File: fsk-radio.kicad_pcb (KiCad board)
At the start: 4 copper layers, 62.5 x 25 mm, 86 parts, among them IC1 STM32F4xx-QFN48, IC2 AT86RF215, IC3 LM3671, IC4 LSM6DS3, IC5 CAT24-SOT23, IC7 DPX202700DT, IC8 74AHC2G04, J1 USB_A, J2 CONN_01X14, J3 CONN_02X05, J4 RF_Shield_One_Piece, J7 SMA, X1 TXETBLSANF-26, X2 32.768kHz

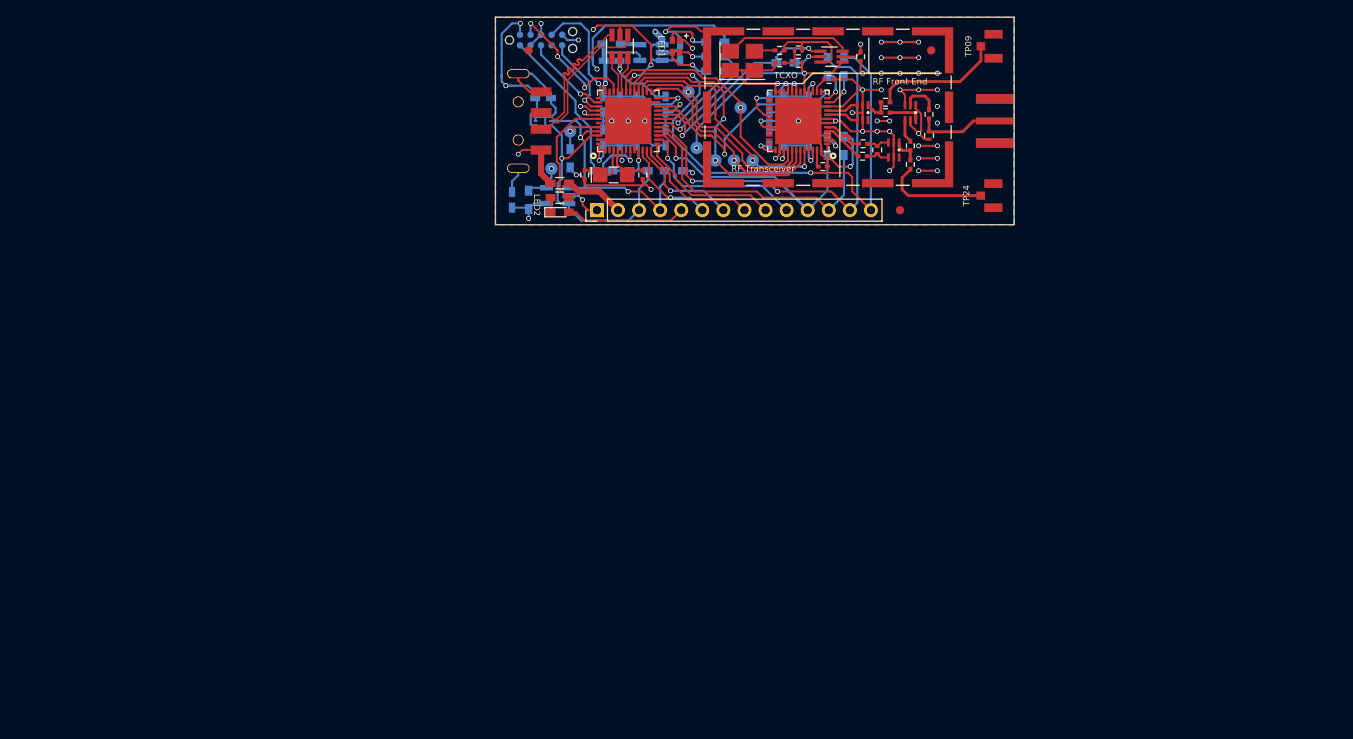
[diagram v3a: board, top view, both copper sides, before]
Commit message: Rework and revise for revision 2.
Major changes include:
  - Refactor clock heirarchy to improve RF performance.
  - Add pushbutton switch and SPI flash.
  - Shrink board dimensions down to make it more of a usable dongle.
  - Eliminate u.FL test points and SPI test pads.
  - Convert pin headers to castellated edges.
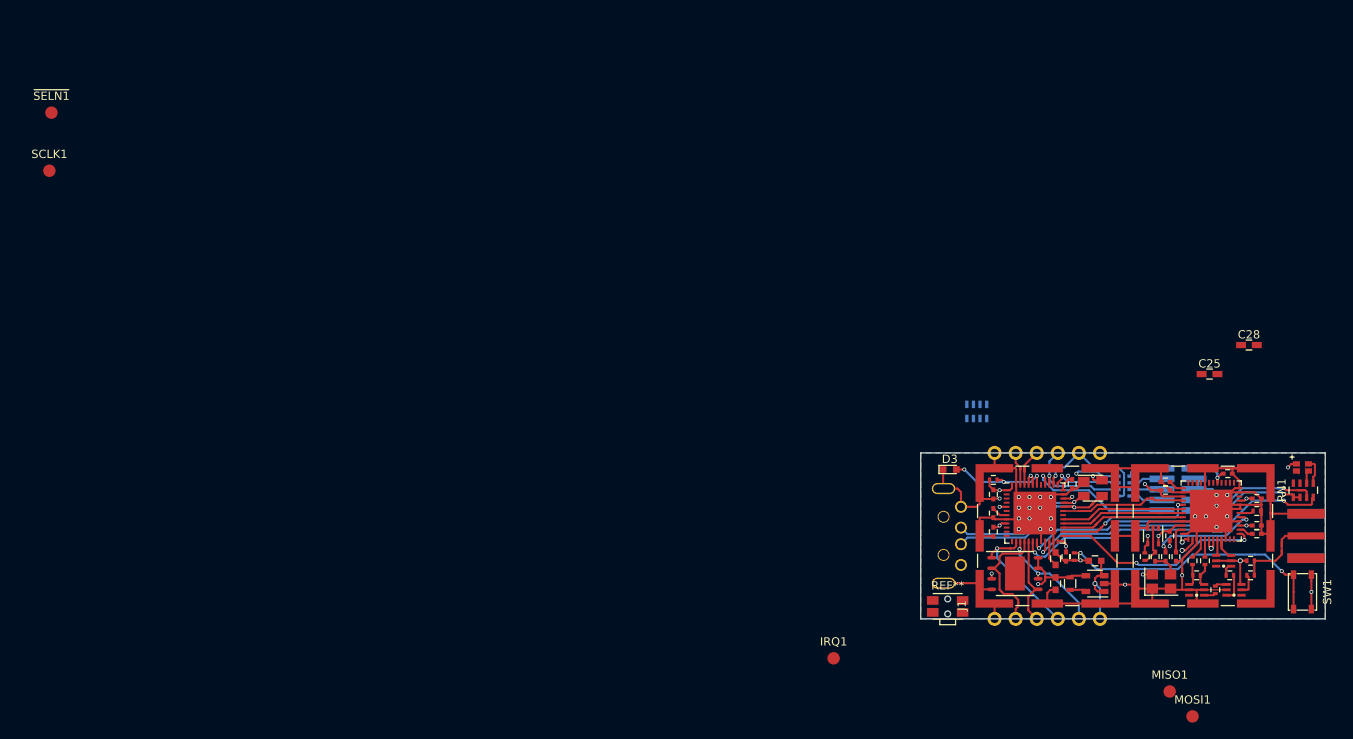
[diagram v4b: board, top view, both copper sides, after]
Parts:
- removed BOOT: BOOT, Measurement_Points:Measurement_Point_Round-SMD-Pad_Small
- removed C1, C2: 1u, Capacitors_SMD:C_0603_HandSoldering
- removed C12, C13, C14, C30: C, Capacitors_SMD:C_0402
- removed C16: C, Capacitors_SMD:C_0603_HandSoldering
- removed IC5: CAT24-SOT23, TO_SOT_Packages_SMD:SOT-23-5_HandSoldering
- removed IC8: 74AHC2G04, TO_SOT_Packages_SMD:SOT-363_SC-70-6_Handsoldering
- removed IRQ, MISO, MOSI, SCLK, TCXO, ~CSEL: TEST, Measurement_Points:Measurement_Point_Round-SMD-Pad_Small
- removed R10, R11: 4.7k, Resistors_SMD:R_0603_HandSoldering
- removed R12, R13: 470k, Resistors_SMD:R_0402
- removed R14, R9: 100k, Resistors_SMD:R_0603_HandSoldering
- removed R15, R16, R18, R19: 0, Resistors_SMD:R_0603_HandSoldering
- removed R6, R7: 270, Resistors_SMD:R_0603_HandSoldering
- removed R8: 100, Resistors_SMD:R_0603_HandSoldering
- removed the REF** at (101.2, 41.5)
- removed the REF** at (146.0, 60.8)
- removed the REF** at (149.8, 41.5)
- removed TP09, TP24: u.FL, FSK Parts:u.FL
- removed WP: WP, Measurement_Points:Measurement_Point_Round-SMD-Pad_Small
- removed X2: 32.768kHz, Crystals:Crystal_SMD_G8-2pin_3.2x1.5mm_HandSoldering
- added IC6: W25Q32BVZPIP, Housings_DFN_QFN:DFN-S-8-1EP_6x5mm_Pitch1.27mm, F.Cu at (159.8, 104.5)
- added IRQ1: TEST, Measurement_Points:Measurement_Point_Round-SMD-Pad_Small, F.Cu at (138.0, 114.8)
- added J5: RF_Shield_One_Piece, Shielding_Cabinets:Laird_Technologies_BMI-S-102_16.50x16.50mm, F.Cu at (163.8, 100.0)
- added J6: Conn_01x06, FSK Parts:Castellated_Edge_6pin_2.54mm, F.Cu at (163.8, 110.0)
- added MISO1: TEST, Measurement_Points:Measurement_Point_Round-SMD-Pad_Small, F.Cu at (178.5, 118.8)
- added MOSI1: TEST, Measurement_Points:Measurement_Point_Round-SMD-Pad_Small, F.Cu at (181.2, 121.8)
- added REF**: SW_SPST_EVQP7C, Buttons_Switches_SMD:SW_SPST_EVQP7C, F.Cu at (151.8, 108.5)
- added RN1: 330, Resistors_SMD:R_Array_Concave_4x0603, F.Cu at (194.6, 94.5)
- added RN2: 4.7k, Resistors_SMD:R_Array_Concave_4x0603, B.Cu at (155.2, 85.0)
- added RN3: 22, Resistors_SMD:R_Array_Concave_4x0603, B.Cu at (173.0, 94.0)
- added SCLK1: TEST, Measurement_Points:Measurement_Point_Round-SMD-Pad_Small, F.Cu at (43.5, 56.0)
- added SW1: SW_Push, Buttons_Switches_SMD:SW_SPST_PTS810, F.Cu at (194.5, 106.8)
- added ~SELN1: TEST, Measurement_Points:Measurement_Point_Round-SMD-Pad_Small, F.Cu at (43.8, 49.0)
- C10, C18, C21, C22, C23, C24, C5, C6, C8: footprint Capacitors_SMD:C_0603_HandSoldering -> Capacitors_SMD:C_0402; moved to F.Cu
- C11: value 2.2u -> 4.7u; footprint Capacitors_SMD:C_0603_HandSoldering -> Capacitors_SMD:C_0603; moved to F.Cu
- C25, C28: moved to F.Cu
- C26, C27, C29, C31, C32: footprint Capacitors_SMD:C_0402 -> Inductors_SMD:L_0402
- C3, C7: footprint Capacitors_SMD:C_0603_HandSoldering -> Capacitors_SMD:C_0603; moved to F.Cu
- C9: value 2.2u -> 1n; footprint Capacitors_SMD:C_0603_HandSoldering -> Capacitors_SMD:C_0402; moved to F.Cu
- D2: value ESDALCL6 -> PRTR5V0U2X; footprint TO_SOT_Packages_SMD:SOT-23-6_Handsoldering -> TO_SOT_Packages_SMD:SOT-143
- D3: footprint LEDs:LED_0603_HandSoldering -> LEDs:LED_0603
- IC1, IC2: footprint FSK Parts:QFN48 -> Housings_DFN_QFN:QFN-48-1EP_7x7mm_Pitch0.5mm
- IC3: footprint TO_SOT_Packages_SMD:SOT-23-5_HandSoldering -> TO_SOT_Packages_SMD:SOT-23-5; moved to F.Cu
- IC4: value LSM6DS3 -> NC7SZ04; footprint FSK Parts:LGA-14 -> TO_SOT_Packages_SMD:SOT-353_SC-70-5; moved to F.Cu
- J1: footprint FSK Parts:USB-A-Plug -> FSK Parts:CUI-UP2-AH-TH
- J2: value CONN_01X14 -> Conn_01x06; footprint Pin_Headers:Pin_Header_Straight_1x14_Pitch2.54mm -> FSK Parts:Castellated_Edge_6pin_2.54mm; moved to B.Cu
- J3: footprint Connectors:Tag-Connect_TC2050-IDC-NL -> FSK Parts:ftsh-105-01-dv
- J4: footprint Shielding_Cabinets:Laird_Technologies_BMI-S-209-F_29.36x18.50mm -> Shielding_Cabinets:Laird_Technologies_BMI-S-102_16.50x16.50mm
- L1: footprint Inductors_SMD:L_0603_HandSoldering -> Inductors_SMD:L_0603; moved to F.Cu
- R1: value 0 -> 10k; footprint Resistors_SMD:R_0603_HandSoldering -> Resistors_SMD:R_0402
- R2: footprint Resistors_SMD:R_0603_HandSoldering -> Resistors_SMD:R_0402
- R3, R4: value 100k -> R; footprint Resistors_SMD:R_0603_HandSoldering -> Resistors_SMD:R_0402; moved to F.Cu
- X1: footprint Crystals:Crystal_SMD_TXC_7M-4pin_3.2x2.5mm_HandSoldering -> Crystals:Crystal_SMD_3225-4pin_3.2x2.5mm
- moved J3 93.9 mm to (179.5, 94.4), turned to 180 degrees
- moved D1 91.0 mm to (194.5, 91.8), turned to 270 degrees
- moved C18 89.0 mm to (178.5, 100.0), turned to 270 degrees
- moved IC4 88.9 mm to (176.5, 100.0), turned to 270 degrees
- moved R4 88.8 mm to (189.0, 97.0), turned to 0 degrees
- moved C10 88.2 mm to (189.0, 98.8), turned to 0 degrees
- moved L1 85.3 mm to (166.5, 105.8), turned to 90 degrees
- moved IC3 83.4 mm to (169.5, 105.8)
- moved C3 82.7 mm to (164.8, 105.8), turned to 270 degrees
- moved X1 80.5 mm to (177.5, 105.5)
- moved C7 79.1 mm to (169.5, 103.0), turned to 180 degrees
- moved D2 78.0 mm to (169.2, 94.2), turned to 0 degrees
- moved C9 77.7 mm to (176.8, 102.5)
- moved C15 76.7 mm to (178.0, 102.5), turned to 270 degrees
- moved R1 76.6 mm to (167.0, 102.5), turned to 270 degrees
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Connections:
- C15 pad 1: Net-(C15-Pad1) -> /CPU/RF_CLK
- C4 pad 1: Net-(B24-Pad1) -> GND
- C9 pad 1: Net-(C11-Pad1) -> Net-(C9-Pad1)
- C9 pad 2: GND -> Net-(C15-Pad2)
- D2 pad 1: /CPU/USB+ -> GND
- D2 pad 2: GND -> /CPU/USB+
- D2 pad 4: /CPU/USBA- -> +5V
- D3 pad 1: Net-(D3-Pad1) -> GND
- D3 pad 2: VCC -> /CPU/STATUS
- IC1 pad 12: /CPU/PA2 -> Net-(IC1-Pad12)
- IC1 pad 13: /CPU/PA3 -> Net-(IC1-Pad13)
- IC1 pad 14: /CPU/PA4 -> /CPU/~FL_CSEL
- IC1 pad 15: /CPU/PA5 -> /CPU/FL_SCLK
- IC1 pad 16: /CPU/PA6 -> /CPU/FL_MISO
- IC1 pad 17: /CPU/PA7 -> /CPU/FL_MOSI
- IC1 pad 18: Net-(IC1-Pad18) -> /CPU/RED
- IC1 pad 19: Net-(IC1-Pad19) -> /CPU/GREEN
- IC1 pad 20: /CPU/~CLKEN -> GND
- IC1 pad 21: /CPU/~RF_NRST -> /CPU/BLUE
- IC1 pad 25: /CPU/~SPI_CS -> /CPU/~RF_NRST
- IC1 pad 29: /CPU/PA8 -> /CPU/~SPI_CS
- IC1 pad 30: Net-(D2-Pad5) -> +5V
- IC1 pad 38: Net-(IC1-Pad38) -> /CPU/TXD_OUT
- IC1 pad 39: Net-(IC1-Pad39) -> /CPU/RXD_IN
- IC1 pad 42: Net-(IC1-Pad42) -> /CPU/STATUS
- IC1 pad 43: Net-(IC1-Pad43) -> /CPU/SWITCH
- IC1 pad 44: Net-(BOOT1-Pad1) -> /CPU/SWITCH
- IC1 pad 5: TCXO -> Net-(IC1-Pad5)
- IC1 pad 7: ~NRST -> Net-(C4-Pad2)
- IC2 pad 17: TCXO -> /CPU/RF_CLK
- IC4 pad 1: GND -> (no net)
- IC4 pad 2: GND -> Net-(C9-Pad1)
- IC4 pad 4: Net-(IC4-Pad4) -> Net-(IC1-Pad5)
- J1 pad 1: Net-(D2-Pad5) -> +5V
- J1 pad 2: /CPU/USBA- -> /CPU/USB-
- J1 pad 3: /CPU/USBA+ -> /CPU/USB+
- J2 pad 2: +5V -> /CPU/SDA
- J2 pad 3: /CPU/SDA -> /CPU/SCL
- J2 pad 4: /CPU/SCL -> /CPU/RXD_IN
- J2 pad 5: VCC -> /CPU/TXD_OUT
- J2 pad 6: /CPU/PA0 -> VCC
- J3 pad 10: ~NRST -> Net-(IC1-Pad40)
- J3 pad 2: Net-(IC1-Pad34) -> Net-(J3-Pad2)
- J3 pad 4: Net-(IC1-Pad37) -> Net-(J3-Pad4)
- J3 pad 6: Net-(IC1-Pad39) -> Net-(J3-Pad6)
- J3 pad 8: Net-(IC1-Pad38) -> Net-(J3-Pad8)
- R1 pad 1: +5V -> /CPU/SWITCH
- R1 pad 2: Net-(D2-Pad5) -> GND
- R2 pad 1: Net-(D3-Pad1) -> VCC
- R2 pad 2: Net-(IC1-Pad42) -> /CPU/STATUS
- R3 pad 1: GND -> Net-(IC1-Pad5)
- R3 pad 2: /CPU/~CLKEN -> Net-(C9-Pad1)
- R4 pad 1: VCC -> Net-(IC2-Pad18)
- R4 pad 2: ~NRST -> GND
- X1 pad 3: Net-(C15-Pad1) -> Net-(C15-Pad2)
- X1 pad 4: Net-(IC8-Pad6) -> VCC
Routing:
- net /CPU/PA8: track 70.2 -> 0.00 mm, vias 2 -> 0
- net /CPU/PA7: track 51.5 -> 0.00 mm, vias 2 -> 0
- net /CPU/SWITCH: track 0.00 -> 49.4 mm, vias 0 -> 3
- net Net-(D2-Pad5): track 42.8 -> 0.00 mm, vias 4 -> 0
- net /CPU/RED: track 0.00 -> 39.0 mm, vias 0 -> 2
- net TCXO: track 38.9 -> 0.00 mm, vias 3 -> 0
- net /CPU/GREEN: track 0.00 -> 38.3 mm, vias 0 -> 2
- net /CPU/BLUE: track 0.00 -> 35.8 mm, vias 0 -> 2
- net /CPU/PA6: track 35.0 -> 0.00 mm
- net /CPU/PA5: track 34.6 -> 0.00 mm, vias 1 -> 0
- net GND: track 330.0 -> 296.2 mm, vias 49 -> 27
- net Net-(IC1-Pad41): track 30.7 -> 0.00 mm, vias 2 -> 0
- net /CPU/SDA: track 32.4 -> 4.33 mm, vias 1 -> 0
- net /CPU/~CLKEN: track 27.5 -> 0.00 mm, vias 2 -> 0
- net /CPU/SCL: track 31.2 -> 5.05 mm, vias 2 -> 0
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- removed copper zone on F.Cu, net GND
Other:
- board size 62.5 x 25 mm -> 48.8 x 20 mm
- net class Default: clearance 0.18 -> 0.175; via_dia 0.6 -> 0.475; via_drill 0.4 -> 0.3
- net class RF-50ohm removed
- net class RF-Diff removed
- net class USB: clearance 0.15 -> 0.16; trace_width 0.2 -> 0.25; via_dia 0.6 -> 0.475; via_drill 0.4 -> 0.3
- rule pad_to_mask_clearance: 0.05 -> 0
- rule trace_clearance: 0.18 -> 0.175
- rule trace_min: 0.15 -> 0.2
- board text added: "CSEL"
- board text added: "MISO"
- board text added: "MOSI"
- board text added: "RXD_IN"
- board text added: "SCLK"
- board text added: "TXD_OUT"
- board text added: "VUSB"
- board text removed: "+5V"
- board text removed: "A"
- board text removed: "B"
- board text removed: "Blue"
- board text removed: "C"
- board text removed: "CPU Bypass"
- board text removed: "Core Bypass"
- board text removed: "DC-DC Regulator"
- board text removed: "EEPROM"
- board text removed: "FEx09"
- board text removed: "FEx24"
- board text removed: "Green"
- board text removed: "IMU"
- board text removed: "JTAG"
- board text removed: "L"
- board text removed: "LED1"
- board text removed: "LED2"
- board text removed: "PA0"
- board text removed: "PA1"
- board text removed: "PA2"
- board text removed: "PA3"
- board text removed: "PA4"
- board text removed: "PA5"
- board text removed: "PA6"
- board text removed: "PA7"
- board text removed: "PA8"
- board text removed: "RF Bypass"
- board text removed: "RF Front End"
- board text removed: "RF Transceiver"
- board text removed: "Red"
- board text removed: "TCXO"
- board text removed: "https://github.com/oskirby/fsk-radio"

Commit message: Add more test features to the RF section.
Split the RF and CPU power nets and connect them via a zero-ohm jumper
to allow current sense, and add test pads for the RF SPI bus.
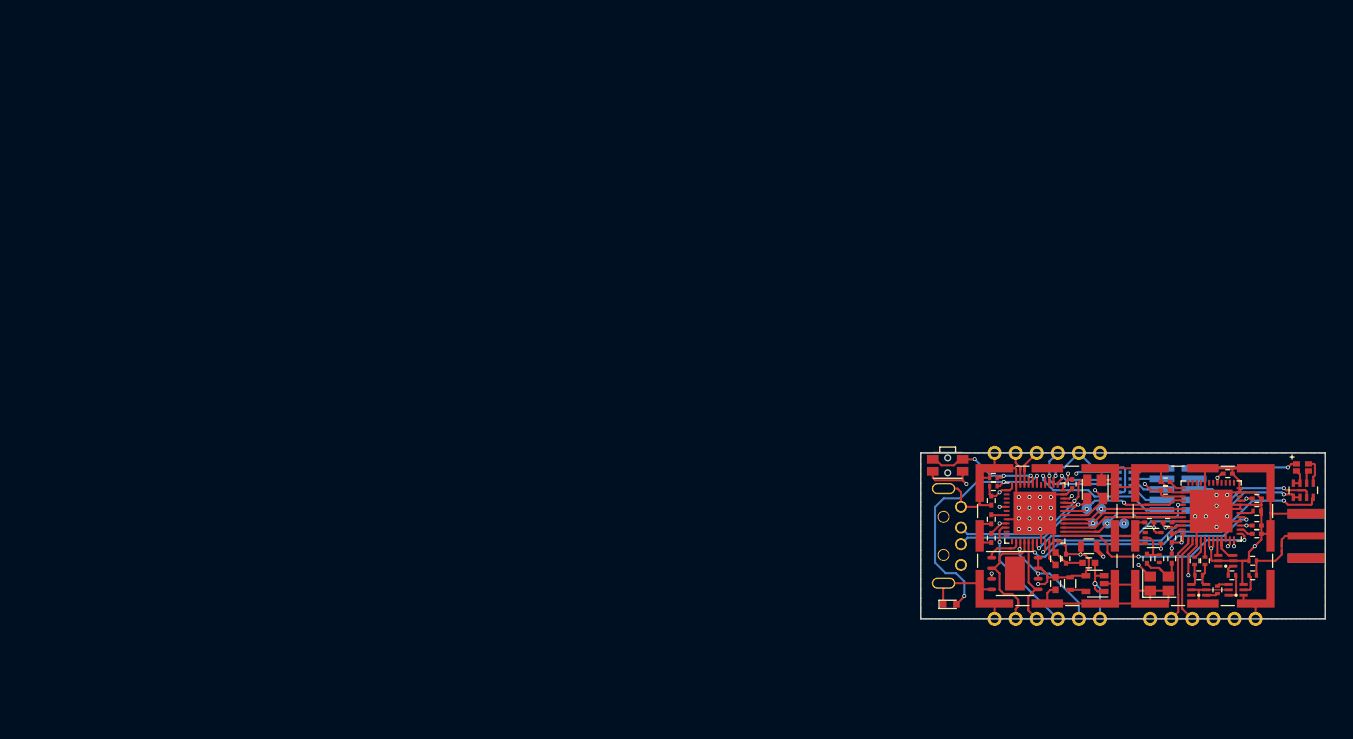
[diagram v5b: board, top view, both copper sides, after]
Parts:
- removed C18: C, Capacitors_SMD:C_0402
- removed REF**: SW_SPST_EVQP7C, Buttons_Switches_SMD:SW_SPST_EVQP7C
- removed RN2: 4.7k, Resistors_SMD:R_Array_Concave_4x0603
- added J8: Conn_01x06, FSK Parts:Castellated_Edge_6pin_2.54mm, F.Cu at (182.5, 110.0)
- added R5: 0, Resistors_SMD:R_0805, F.Cu at (168.8, 101.2)
- added exegin-logo: exegin-logo, FSK Parts:exegin-logo-mask, B.Cu at (193.2, 106.8)
- C25, C28: footprint Capacitors_SMD:C_0603_HandSoldering -> Capacitors_SMD:C_0402
- IRQ1, MISO1, MOSI1, SCLK1, ~SELN1: footprint Measurement_Points:Measurement_Point_Round-SMD-Pad_Small -> FSK Parts:Measurement_Point_Round-SMD-Pad_XSmall; moved to B.Cu
- SW1: footprint Buttons_Switches_SMD:SW_SPST_PTS810 -> Buttons_Switches_SMD:SW_SPST_EVQP7C
- moved ~SELN1 135.2 mm to (170.2, 96.8)
- moved SCLK1 134.4 mm to (171.0, 98.5)
- moved SW1 45.4 mm to (151.8, 91.5), turned to 180 degrees
- moved IRQ1 35.4 mm to (168.5, 96.8)
- moved MOSI1 26.2 mm to (169.2, 98.5)
- moved C10 23.3 mm to (166.0, 102.8), turned to 270 degrees
- moved MISO1 21.0 mm to (173.0, 98.5)
- moved C25 19.1 mm to (189.0, 98.8)
- moved C28 18.5 mm to (189.0, 95.5)
- moved D3 16.2 mm to (152.0, 108.2)
- moved R1 13.6 mm to (157.2, 93.0), turned to 180 degrees
- moved C17 13.3 mm to (176.1, 98.4), turned to 0 degrees
- moved C24 12.9 mm to (178.2, 98.4), turned to 0 degrees
- moved oshw-text 4.12 mm to (177.2, 106.5)
- moved oshw-silks 3.40 mm to (185.5, 105.5)
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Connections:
- net /CPU/PA1 renamed Net-(IC1-Pad11)
- C22 pad 1: VCC -> VDD
- C23 pad 1: VCC -> VDD
- C24 pad 1: VCC -> VDD
- C25 pad 1: VCC -> VDD
- C28 pad 1: VCC -> VDD
- IC1 pad 10: /CPU/PA0 -> /CPU/~EXT_CSEL
- IC2 pad 15: VCC -> VDD
- IC2 pad 21: VCC -> VDD
- IC2 pad 29: VCC -> VDD
- IC2 pad 39: VCC -> VDD
- IC2 pad 46: VCC -> VDD
- J6 pad 4: /CPU/~FL_CSEL -> /CPU/~EXT_CSEL
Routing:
- net VDD: track 0.00 -> 50.1 mm, vias 0 -> 6
- net /CPU/SWITCH: track 49.4 -> 16.9 mm
- net /CPU/STATUS: track 12.7 -> 30.3 mm
- net /CPU/~EXT_CSEL: track 0.00 -> 14.6 mm, vias 0 -> 1
- net /CPU/~FL_CSEL: track 16.8 -> 4.57 mm, vias 1 -> 0
- net VCC: track 149.8 -> 138.2 mm, vias 14 -> 10
- net /RF/FEA09: track 0.00 -> 10.4 mm, vias 0 -> 1
- net /RF/FEB09: track 0.00 -> 9.62 mm, vias 0 -> 1
- net /RF/FEA24: track 0.89 -> 10.5 mm, vias 1 -> 0
- net /RF/FEB24: track 2.10 -> 10.6 mm, vias 1 -> 0
- net GND: track 296.2 -> 289.5 mm, vias 27 -> 26
- net +5V: track 41.1 -> 46.4 mm
- net /CPU/USB+: track 18.1 -> 20.9 mm
- net Net-(C15-Pad2): track 3.10 -> 5.62 mm
- net Net-(D1-PadB): track 0.39 -> 2.84 mm
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- added copper zone on F.Cu, net GND
- added copper zone on In2.Cu, net VDD
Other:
- board text added: "RX"
- board text added: "TX"
- board text removed: "RXD_IN"
- board text removed: "TXD_OUT"

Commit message: Release to manufacturing: rev2 prototype.
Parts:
- added FID1: Fiducial_1mm_Dia_2.54mm_Outer_CopperTop, FSK Parts:Fiducial_1mm_Dia_1.5mm_Outer_CopperTop, F.Cu at (176.0, 95.0)
- added FID2: Fiducial_1mm_Dia_2.54mm_Outer_CopperTop, FSK Parts:Fiducial_1mm_Dia_1.5mm_Outer_CopperTop, F.Cu at (188.8, 93.8)
- added FID2: Fiducial_1mm_Dia_2.54mm_Outer_CopperTop, FSK Parts:Fiducial_1mm_Dia_1.5mm_Outer_CopperTop, F.Cu at (171.0, 103.0)
- moved exegin-logo 0.25 mm to (193.0, 106.8)
- moved oshw-silks 0.25 mm to (185.2, 105.5)
- moved MISO1 0.12 mm to (173.1, 98.5)
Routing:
- net GND: track 289.5 -> 337.8 mm, vias 26 -> 28
- net VCC: track 138.2 -> 129.5 mm, vias 10 -> 11
- net /CPU/STATUS: track 30.3 -> 27.0 mm
- net Net-(IC1-Pad5): track 23.7 -> 25.3 mm
- net VDD: track 50.1 -> 49.0 mm
- net +5V: track 46.4 -> 47.3 mm
- net Net-(C29-Pad1): track 12.8 -> 12.0 mm
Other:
- board text added: "IRQ"
- board text added: "~CS"

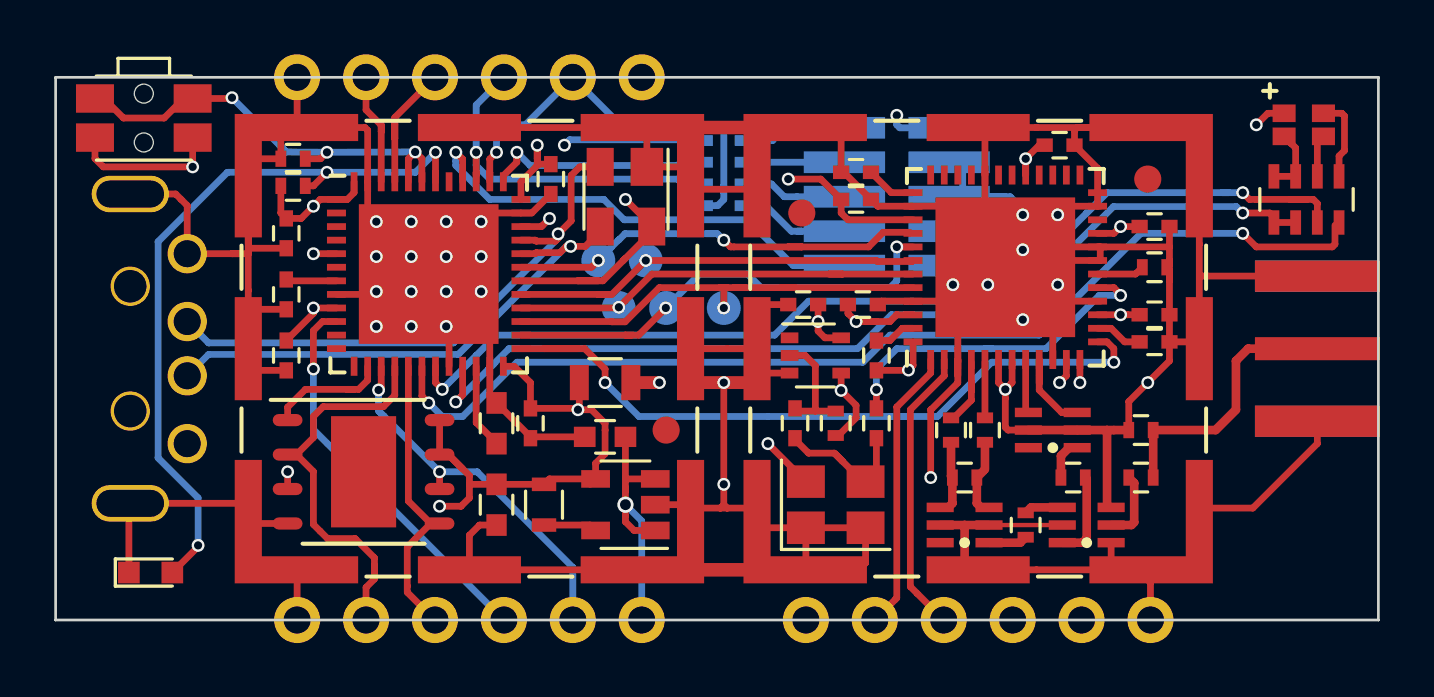
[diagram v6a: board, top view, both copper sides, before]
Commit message: Move 3D models into common repository.
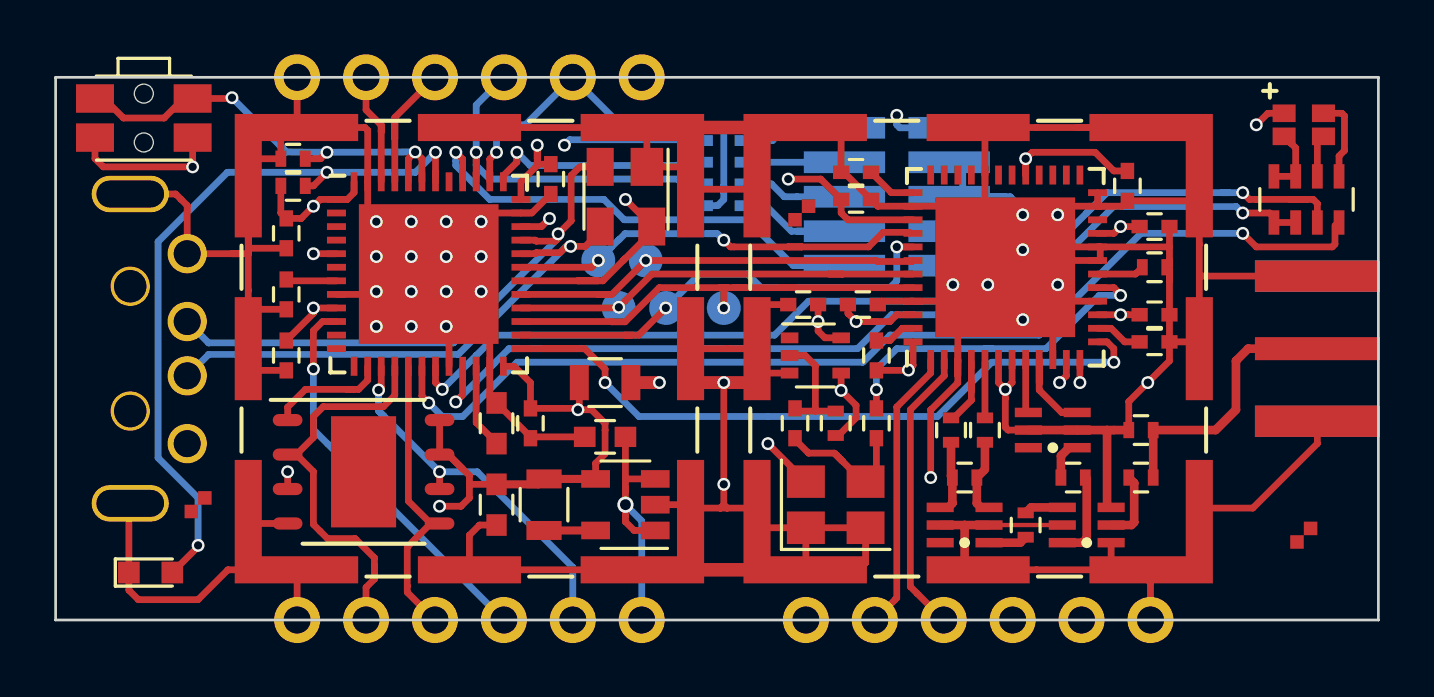
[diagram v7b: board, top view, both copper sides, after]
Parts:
- FID1, FID2 (x2): footprint FSK Parts:Fiducial_1mm_Dia_1.5mm_Outer_CopperTop -> FSK Parts:Fiducial_1mm_checker_1.5mm_mask
- L1: footprint Inductors_SMD:L_0603 -> Inductors_SMD:L_0805
- R3: value R -> R3
- moved FID2 17.5 mm to (153.8, 105.8)
- moved FID2 14.3 mm to (194.5, 106.9)
- moved C22 2.92 mm to (188.0, 94.0), turned to 270 degrees
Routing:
- net VDD: track 49.0 -> 52.2 mm
- net GND: track 337.8 -> 340.5 mm
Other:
- board text added: "https://github.com/ oskirby/pysun-usb"
